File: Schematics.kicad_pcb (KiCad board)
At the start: 2 copper layers, 55.4 x 46.7 mm, 47 parts, among them Q1 AO3400A, Q2 AO3401A

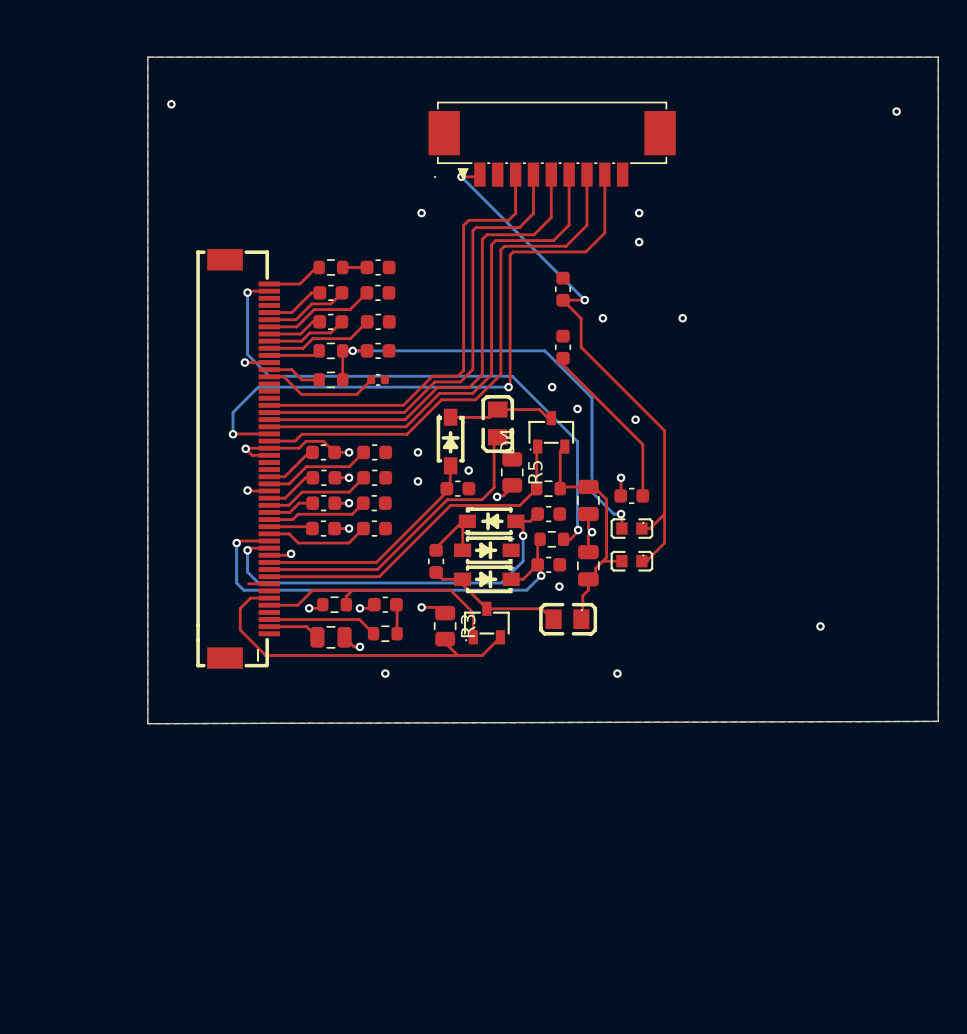
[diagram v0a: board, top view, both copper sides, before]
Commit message: added 50 pin FFC pinsocket for easier testing and soldering
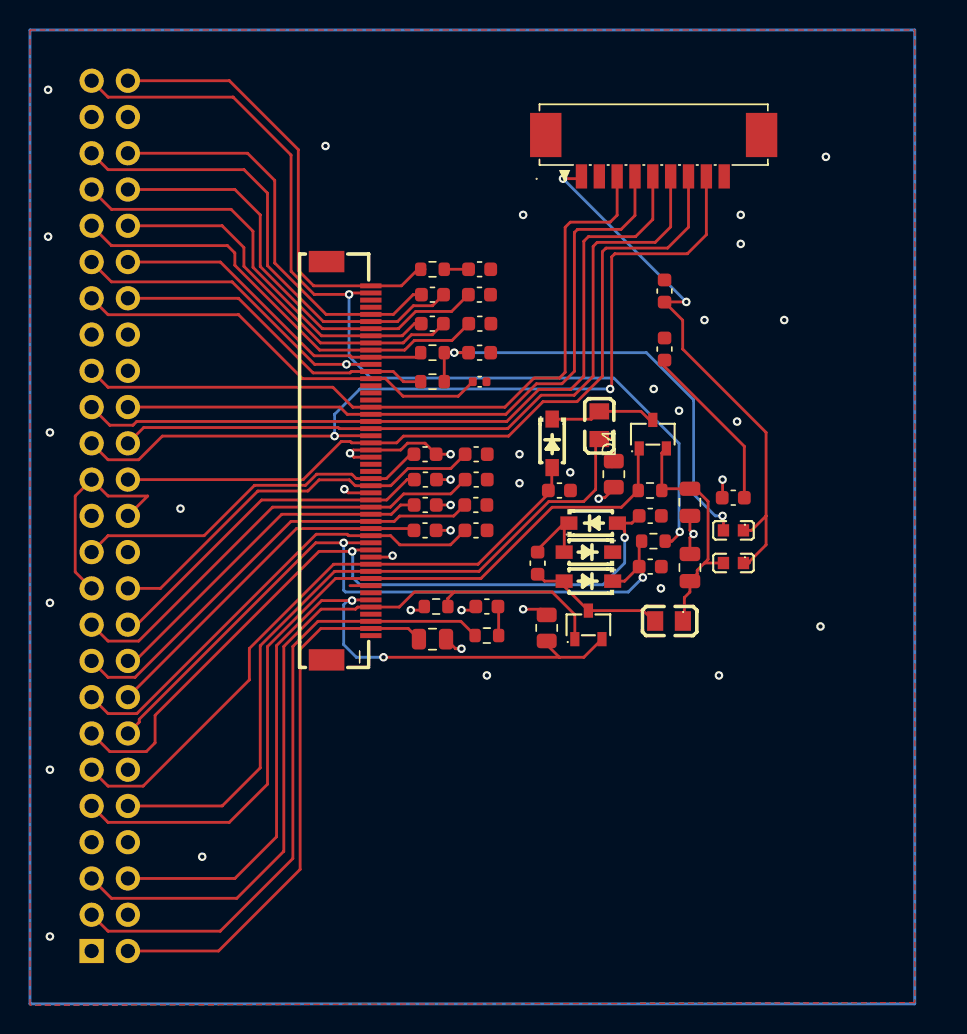
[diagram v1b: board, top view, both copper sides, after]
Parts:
- added REF**: PinHeader_2x25_P2.54mm_Vertical, Connector_PinHeader_2.54mm:PinHeader_2x25_P2.54mm_Vertical, B.Cu at (48.0, 95.4)
- moved C3 7.11 mm to (79.2, 68.2)
- moved C4 7.11 mm to (87.1, 68.5)
- moved C6 7.11 mm to (87.1, 64.9)
- moved C1 7.11 mm to (71.9, 73.5)
- moved C15 7.11 mm to (75.2, 51.4)
- moved C16 7.11 mm to (80.8, 63.1)
- moved C18 7.11 mm to (75.2, 49.4)
- moved C20 7.11 mm to (71.9, 49.4)
- moved C24 7.11 mm to (88.1, 53.2)
- moved C25 7.11 mm to (88.1, 49.1)
- moved C31 7.11 mm to (71.4, 60.6)
- moved C7 7.11 mm to (74.9, 65.9)
- moved C8 7.11 mm to (71.4, 65.9)
- moved D1 7.11 mm to (82.8, 69.5)
- moved D3 7.11 mm to (82.8, 67.4)
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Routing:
- net /FPL_VCOM: track 7.74 -> 45.5 mm
- net /GDRH: track 18.3 -> 55.3 mm
- net GND: track 29.4 -> 65.2 mm, vias 32 -> 40
- net /TFT_VCOM: track 3.68 -> 39.1 mm
- net /GDRC: track 24.3 -> 57.0 mm
- net /RESEH: track 24.8 -> 56.9 mm, vias 0 -> 2
- net /VGH: track 39.0 -> 68.0 mm
- net /RESEC: track 25.2 -> 54.0 mm
- net /VCOMBD: track 4.29 -> 32.2 mm
- net /VPC: track 16.4 -> 44.2 mm
- net /CP1N: track 5.87 -> 33.3 mm
- net /VGL: track 28.2 -> 53.7 mm
- net /CP2P: track 3.88 -> 29.2 mm
- net /VSH: track 7.28 -> 32.6 mm
- net /CP1P: track 4.51 -> 29.6 mm
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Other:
- board outline removed

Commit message: added a missing capacitor
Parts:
- added C29: CL31A107MQHNNNE, local:C1206, F.Cu at (93.0, 72.5)
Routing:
- net V_B: track 17.2 -> 20.2 mm
